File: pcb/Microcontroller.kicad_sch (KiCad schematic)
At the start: 39 parts, among them J1 PDI, SW2 START, SW3 STOP, U3 ATxmega16A4U-A, Y1 8MHz

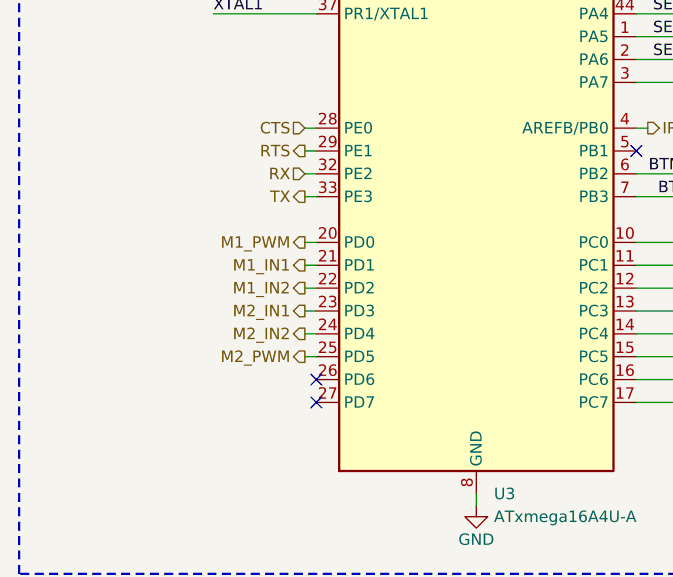
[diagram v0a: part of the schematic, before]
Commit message: [pcb] Line sensors placed
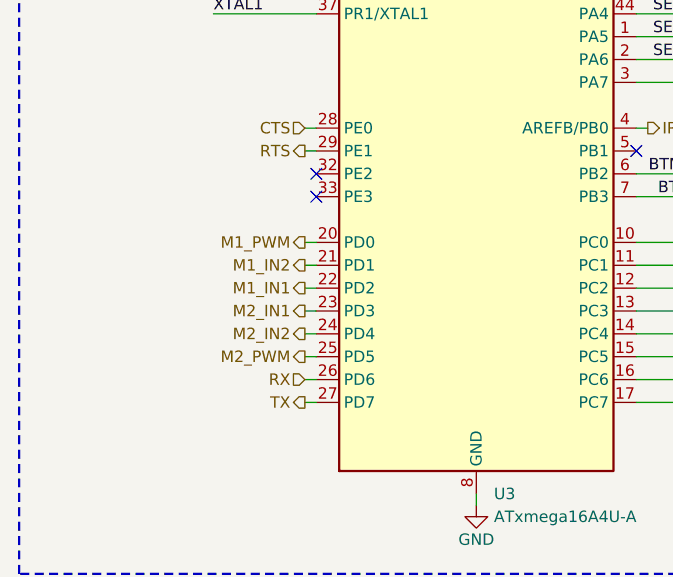
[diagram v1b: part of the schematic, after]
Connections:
- net M1_IN1: now also U3.22 (PD2); no longer U3.21 (PD1)
- net M1_IN2: now also U3.21 (PD1); no longer U3.22 (PD2)
- net RX: now also U3.26 (PD6); no longer U3.32 (PE2)
- net TX: now also U3.27 (PD7); no longer U3.33 (PE3)
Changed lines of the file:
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@@
   (junction (at 148.59 95.25) (diameter 0) (color 0 0 0 0)
   )
-  (no_connect (at 50.8 102.87))
   (no_connect (at 86.36 77.47))
+  (no_connect (at 50.8 80.01))
   (no_connect (at 135.89 39.37))
   (no_connect (at 148.59 39.37))
-  (no_connect (at 50.8 105.41))
+  (no_connect (at 50.8 82.55))
   (bus_entry (at 96.52 62.23) (size 2.54 -2.54)
     (stroke (width 0) (type default))
@@
     (stroke (width 0) (type default))
   )
+  (wire (pts (xy 49.53 102.87) (xy 50.8 102.87))
+    (stroke (width 0) (type default))
+  )
   (wire (pts (xy 49.53 46.99) (xy 49.53 52.07))
     (stroke (width 0) (type default))
@@
     (stroke (width 0) (type default))
   )
+  (wire (pts (xy 49.53 105.41) (xy 50.8 105.41))
+    (stroke (width 0) (type default))
+  )
   (bus (pts (xy 99.06 52.07) (xy 99.06 54.61))
     (stroke (width 0) (type default))
@@
     (stroke (width 0) (type default))
   )
-  (wire (pts (xy 49.53 82.55) (xy 50.8 82.55))
-    (stroke (width 0) (type default))
-  )
   (wire (pts (xy 205.74 49.53) (xy 218.44 49.53))
     (stroke (width 0) (type default))
@@
   )
   (wire (pts (xy 86.36 102.87) (xy 96.52 102.87))
-    (stroke (width 0) (type default))
-  )
-  (wire (pts (xy 49.53 80.01) (xy 50.8 80.01))
     (stroke (width 0) (type default))
   )
@@
     (effects (font (size 1.27 1.27)) (justify right))
   )
-  (hierarchical_label "RX" (shape input) (at 49.53 80.01 180) (fields_autoplaced)
+  (hierarchical_label "RX" (shape input) (at 49.53 102.87 180) (fields_autoplaced)
     (effects (font (size 1.27 1.27)) (justify right))
   )
@@
     (effects (font (size 1.27 1.27)) (justify right))
   )
-  (hierarchical_label "M1_IN2" (shape output) (at 49.53 92.71 180) (fields_autoplaced)
+  (hierarchical_label "M1_IN2" (shape output) (at 49.53 90.17 180) (fields_autoplaced)
     (effects (font (size 1.27 1.27)) (justify right))
   )
@@
     (effects (font (size 1.27 1.27)) (justify left))
   )
-  (hierarchical_label "TX" (shape output) (at 49.53 82.55 180) (fields_autoplaced)
+  (hierarchical_label "TX" (shape output) (at 49.53 105.41 180) (fields_autoplaced)
     (effects (font (size 1.27 1.27)) (justify right))
   )
@@
     (effects (font (size 1.27 1.27)) (justify left))
   )
-  (hierarchical_label "M1_IN1" (shape output) (at 49.53 90.17 180) (fields_autoplaced)
-    (effects (font (size 1.27 1.27)) (justify right))
-  )
+  (hierarchical_label "M1_IN1" (shape output) (at 49.53 92.71 180) (fields_autoplaced)
+    (effects (font (size 1.27 1.27)) (justify right))
+  )

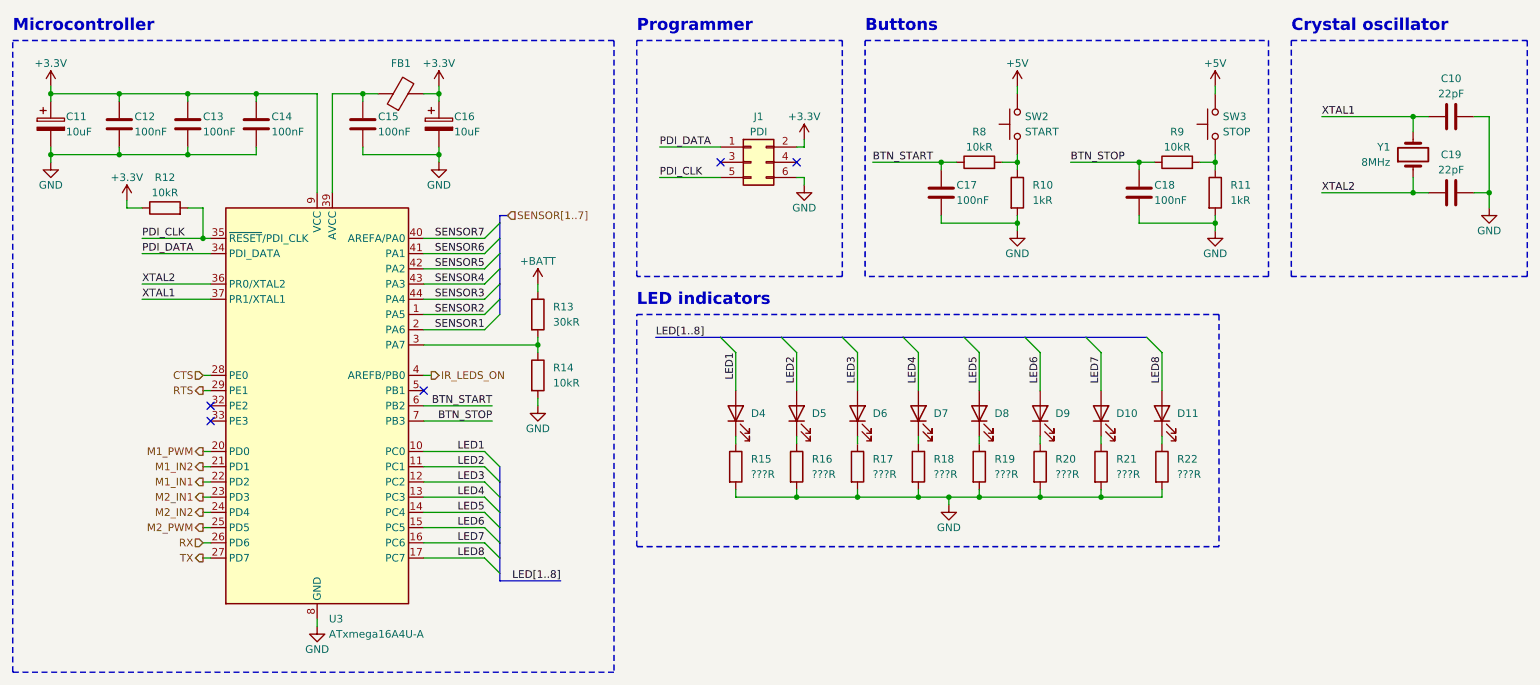
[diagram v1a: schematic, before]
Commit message: [pcb] Trying to minimize number of vias
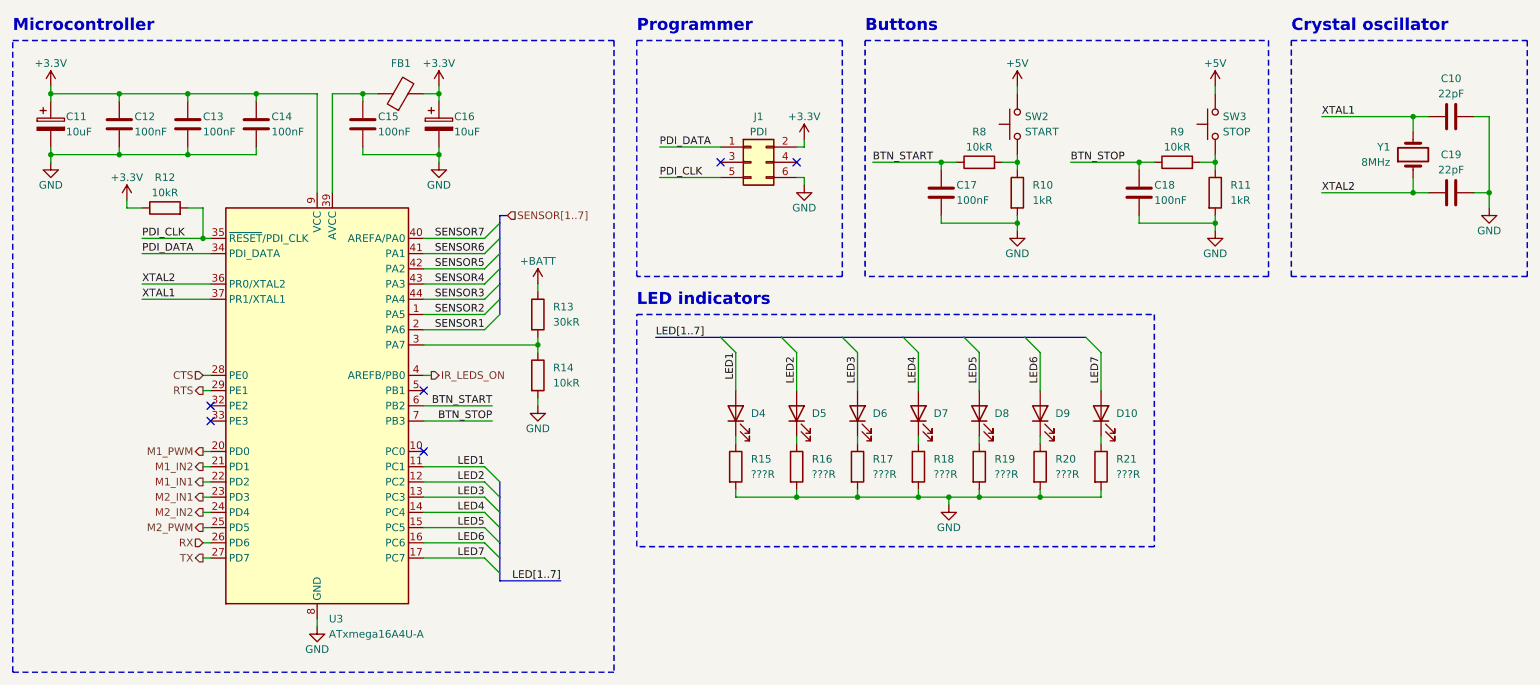
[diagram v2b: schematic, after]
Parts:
- removed D11: YELLOW, LED_SMD:LED_0805_2012Metric, symbol Device:LED
- removed R22: ???R, Resistor_SMD:R_0805_2012Metric, symbol Device:R
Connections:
- net LED8 is gone; now on net LED7: U3.17 (PC7)
- net LED1: now also U3.11 (PC1); no longer U3.10 (PC0)
- net LED2: now also U3.12 (PC2); no longer U3.11 (PC1)
- net LED3: now also U3.13 (PC3); no longer U3.12 (PC2)
- net LED4: now also U3.14 (PC4); no longer U3.13 (PC3)
- net LED5: now also U3.15 (PC5); no longer U3.14 (PC4)
- net LED6: now also U3.16 (PC6); no longer U3.15 (PC5)
- net LED7: no longer U3.16 (PC6)
- no-connect marks 5 -> 6

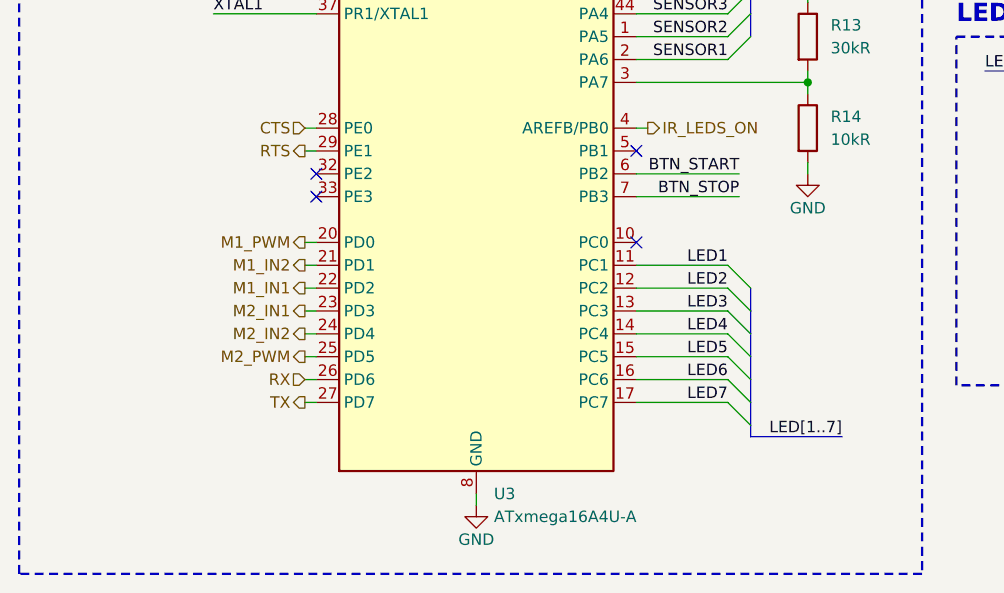
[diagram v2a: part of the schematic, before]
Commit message: [pcb] Rotate uC by 45 deg
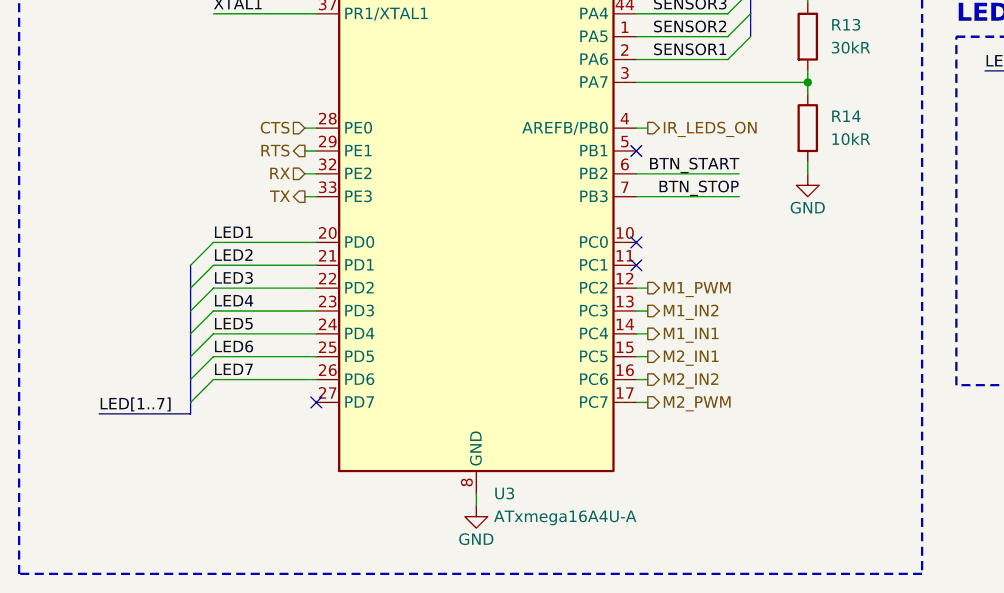
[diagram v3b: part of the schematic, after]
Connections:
- net LED1: now also U3.20 (PD0); no longer U3.11 (PC1)
- net LED2: now also U3.21 (PD1); no longer U3.12 (PC2)
- net LED3: now also U3.22 (PD2); no longer U3.13 (PC3)
- net LED4: now also U3.23 (PD3); no longer U3.14 (PC4)
- net LED5: now also U3.24 (PD4); no longer U3.15 (PC5)
- net LED6: now also U3.25 (PD5); no longer U3.16 (PC6)
- net LED7: now also U3.26 (PD6); no longer U3.17 (PC7)
- net M1_IN1: now also U3.14 (PC4); no longer U3.22 (PD2)
- net M1_IN2: now also U3.13 (PC3); no longer U3.21 (PD1)
- net M1_PWM: now also U3.12 (PC2); no longer U3.20 (PD0)
- net M2_IN1: now also U3.15 (PC5); no longer U3.23 (PD3)
- net M2_IN2: now also U3.16 (PC6); no longer U3.24 (PD4)
- net M2_PWM: now also U3.17 (PC7); no longer U3.25 (PD5)
- net RX: now also U3.32 (PE2); no longer U3.26 (PD6)
- net TX: now also U3.33 (PE3); no longer U3.27 (PD7)

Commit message: [pcb] Remove unnecessary capacitors
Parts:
- removed C11: 10uF, Capacitor_Tantalum_SMD:CP_EIA-3216-18_Kemet-A, symbol Device:C_Polarized
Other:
- moved on the sheet: R12
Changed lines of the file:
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@@
   (junction (at 88.9 38.1) (diameter 0) (color 0 0 0 0)
   )
+  (junction (at 35.56 27.94) (diameter 0) (color 0 0 0 0)
+  )
+  (junction (at 76.2 27.94) (diameter 0) (color 0 0 0 0)
+  )
+  (junction (at 251.46 31.75) (diameter 0) (color 0 0 0 0)
+  )
+  (junction (at 185.42 39.37) (diameter 0) (color 0 0 0 0)
+  )
+  (junction (at 58.42 27.94) (diameter 0) (color 0 0 0 0)
+  )
   (junction (at 35.56 38.1) (diameter 0) (color 0 0 0 0)
   )
-  (junction (at 76.2 27.94) (diameter 0) (color 0 0 0 0)
-  )
-  (junction (at 251.46 31.75) (diameter 0) (color 0 0 0 0)
-  )
-  (junction (at 185.42 39.37) (diameter 0) (color 0 0 0 0)
-  )
-  (junction (at 58.42 27.94) (diameter 0) (color 0 0 0 0)
-  )
   (junction (at 88.9 27.94) (diameter 0) (color 0 0 0 0)
   )
-  (junction (at 35.56 27.94) (diameter 0) (color 0 0 0 0)
-  )
   (junction (at 179.07 95.25) (diameter 0) (color 0 0 0 0)
   )
@@
   (junction (at 218.44 49.53) (diameter 0) (color 0 0 0 0)
   )
-  (junction (at 24.13 27.94) (diameter 0) (color 0 0 0 0)
-  )
   (junction (at 189.23 95.25) (diameter 0) (color 0 0 0 0)
   )
@@
   )
   (junction (at 185.42 49.53) (diameter 0) (color 0 0 0 0)
-  )
-  (junction (at 24.13 38.1) (diameter 0) (color 0 0 0 0)
   )
   (junction (at 148.59 95.25) (diameter 0) (color 0 0 0 0)
@@
     (stroke (width 0) (type default))
   )
-  (wire (pts (xy 24.13 27.94) (xy 24.13 29.21))
-    (stroke (width 0) (type default))
-  )
   (wire (pts (xy 35.56 27.94) (xy 46.99 27.94))
     (stroke (width 0) (type default))
@@
     (stroke (width 0) (type default))
   )
-  (wire (pts (xy 36.83 45.72) (xy 36.83 46.99))
+  (wire (pts (xy 24.13 46.99) (xy 24.13 48.26))
     (stroke (width 0) (type default))
   )
@@
     (stroke (width 0) (type default))
   )
-  (wire (pts (xy 24.13 38.1) (xy 24.13 39.37))
-    (stroke (width 0) (type default))
-  )
   (wire (pts (xy 158.75 93.98) (xy 158.75 95.25))
     (stroke (width 0) (type default))
@@
     (stroke (width 0) (type default))
   )
-  (wire (pts (xy 35.56 38.1) (xy 24.13 38.1))
-    (stroke (width 0) (type default))
-  )
   (wire (pts (xy 46.99 29.21) (xy 46.99 27.94))
     (stroke (width 0) (type default))
@@
     (stroke (width 0) (type default))
   )
-  (wire (pts (xy 46.99 46.99) (xy 49.53 46.99))
+  (wire (pts (xy 34.29 48.26) (xy 49.53 48.26))
     (stroke (width 0) (type default))
   )
@@
     (stroke (width 0) (type default))
   )
-  (wire (pts (xy 49.53 46.99) (xy 49.53 52.07))
+  (wire (pts (xy 49.53 48.26) (xy 49.53 52.07))
     (stroke (width 0) (type default))
   )
@@
     (stroke (width 0) (type default))
   )
-  (wire (pts (xy 24.13 27.94) (xy 35.56 27.94))
-    (stroke (width 0) (type default))
-  )
   (wire (pts (xy 86.36 82.55) (xy 97.79 82.55))
     (stroke (width 0) (type default))
@@
     (stroke (width 0) (type default))
   )
+  (wire (pts (xy 35.56 38.1) (xy 35.56 39.37))
+    (stroke (width 0) (type default))
+  )
   (wire (pts (xy 105.41 59.69) (xy 105.41 60.96))
     (stroke (width 0) (type default))
@@
     (stroke (width 0) (type default))
   )
-  (wire (pts (xy 24.13 36.83) (xy 24.13 38.1))
-    (stroke (width 0) (type default))
-  )
   (wire (pts (xy 179.07 95.25) (xy 189.23 95.25))
     (stroke (width 0) (type default))
@@
     (stroke (width 0) (type default))
   )
-  (wire (pts (xy 36.83 46.99) (xy 39.37 46.99))
+  (wire (pts (xy 24.13 48.26) (xy 26.67 48.26))
     (stroke (width 0) (type default))
   )
@@
     (stroke (width 0) (type default))
   )
+  (wire (pts (xy 35.56 26.67) (xy 35.56 27.94))
+    (stroke (width 0) (type default))
+  )
   (bus (pts (xy 36.83 95.25) (xy 36.83 97.79))
     (stroke (width 0) (type default))
@@
   )
   (wire (pts (xy 96.52 59.69) (xy 86.36 59.69))
-    (stroke (width 0) (type default))
-  )
-  (wire (pts (xy 24.13 26.67) (xy 24.13 27.94))
     (stroke (width 0) (type default))
   )
@@
     )
   )
-  (symbol (lib_id "power:GND") (at 24.13 39.37 0) (unit 1)
-    (in_bom yes) (on_board yes) (dnp no)
-    (property "Reference" "#PWR018" (at 24.13 45.72 0)
-      (effects (font (size 1.27 1.27)) hide)
-    )
-    (property "Value" "GND" (at 24.13 43.18 0)
-      (effects (font (size 1.27 1.27)))
-    )
-    (property "Footprint" "" (at 24.13 39.37 0)
-      (effects (font (size 1.27 1.27)) hide)
-    )
-    (property "Datasheet" "" (at 24.13 39.37 0)
+  (symbol (lib_id "power:GND") (at 35.56 39.37 0) (unit 1)
+    (in_bom yes) (on_board yes) (dnp no)
+    (property "Reference" "#PWR018" (at 35.56 45.72 0)
+      (effects (font (size 1.27 1.27)) hide)
+    )
+    (property "Value" "GND" (at 35.56 43.18 0)
+      (effects (font (size 1.27 1.27)))
+    )
+    (property "Footprint" "" (at 35.56 39.37 0)
+      (effects (font (size 1.27 1.27)) hide)
+    )
+    (property "Datasheet" "" (at 35.56 39.37 0)
       (effects (font (size 1.27 1.27)) hide)
     )
@@
     )
   )
-  (symbol (lib_id "Device:R") (at 43.18 46.99 90) (unit 1)
-    (in_bom yes) (on_board yes) (dnp no)
-    (property "Reference" "R12" (at 43.18 41.91 90)
-      (effects (font (size 1.27 1.27)))
-    )
-    (property "Value" "10kR" (at 43.18 44.45 90)
-      (effects (font (size 1.27 1.27)))
-    )
-    (property "Footprint" "Resistor_SMD:R_0805_2012Metric" (at 43.18 48.768 90)
-      (effects (font (size 1.27 1.27)) hide)
-    )
-    (property "Datasheet" "~" (at 43.18 46.99 0)
+  (symbol (lib_id "Device:R") (at 30.48 48.26 90) (unit 1)
+    (in_bom yes) (on_board yes) (dnp no)
+    (property "Reference" "R12" (at 30.48 43.18 90)
+      (effects (font (size 1.27 1.27)))
+    )
+    (property "Value" "10kR" (at 30.48 45.72 90)
+      (effects (font (size 1.27 1.27)))
+    )
+    (property "Footprint" "Resistor_SMD:R_0805_2012Metric" (at 30.48 50.038 90)
+      (effects (font (size 1.27 1.27)) hide)
+    )
+    (property "Datasheet" "~" (at 30.48 48.26 0)
       (effects (font (size 1.27 1.27)) hide)
     )
@@
     )
   )
-  (symbol (lib_id "Device:C_Polarized") (at 24.13 33.02 0) (unit 1)
-    (in_bom yes) (on_board yes) (dnp no)
-    (property "Reference" "C11" (at 26.67 31.75 0)
-      (effects (font (size 1.27 1.27)) (justify left))
-    )
-    (property "Value" "10uF" (at 26.67 34.29 0)
-      (effects (font (size 1.27 1.27)) (justify left))
-    )
-    (property "Footprint" "Capacitor_Tantalum_SMD:CP_EIA-3216-18_Kemet-A" (at 25.0952 36.83 0)
-      (effects (font (size 1.27 1.27)) hide)
-    )
-    (property "Datasheet" "~" (at 24.13 33.02 0)
-      (effects (font (size 1.27 1.27)) hide)
-    )
-    (pin "1")
-    (pin "2")
-    (instances
-      (project "Autko"
-        (path "/8d5cfdec-de34-4148-9100-7125640c46f5/bbdb254f-809b-458f-9d25-868d15ad41c7"
-          (reference "C11") (unit 1)
-        )
-      )
-    )
-  )
-  (symbol (lib_id "power:+3.3V") (at 36.83 45.72 0) (unit 1)
+  (symbol (lib_id "power:+3.3V") (at 24.13 46.99 0) (unit 1)
     (in_bom yes) (on_board yes) (dnp no) (fields_autoplaced)
-    (property "Reference" "#PWR021" (at 36.83 49.53 0)
-      (effects (font (size 1.27 1.27)) hide)
-    )
-    (property "Value" "+3.3V" (at 36.83 41.91 0)
-      (effects (font (size 1.27 1.27)))
-    )
-    (property "Footprint" "" (at 36.83 45.72 0)
-      (effects (font (size 1.27 1.27)) hide)
-    )
-    (property "Datasheet" "" (at 36.83 45.72 0)
+    (property "Reference" "#PWR021" (at 24.13 50.8 0)
+      (effects (font (size 1.27 1.27)) hide)
+    )
+    (property "Value" "+3.3V" (at 24.13 43.18 0)
+      (effects (font (size 1.27 1.27)))
+    )
+    (property "Footprint" "" (at 24.13 46.99 0)
+      (effects (font (size 1.27 1.27)) hide)
+    )
+    (property "Datasheet" "" (at 24.13 46.99 0)
       (effects (font (size 1.27 1.27)) hide)
     )
@@
     )
   )
-  (symbol (lib_id "power:+3.3V") (at 24.13 26.67 0) (unit 1)
+  (symbol (lib_id "power:+3.3V") (at 35.56 26.67 0) (unit 1)
     (in_bom yes) (on_board yes) (dnp no) (fields_autoplaced)
-    (property "Reference" "#PWR013" (at 24.13 30.48 0)
-      (effects (font (size 1.27 1.27)) hide)
-    )
-    (property "Value" "+3.3V" (at 24.13 22.86 0)
-      (effects (font (size 1.27 1.27)))
-    )
-    (property "Footprint" "" (at 24.13 26.67 0)
-      (effects (font (size 1.27 1.27)) hide)
-    )
-    (property "Datasheet" "" (at 24.13 26.67 0)
-      (effects (font (size 1.27 1.27)) hide)
-    )
+    (property "Reference" "#PWR013" (at 35.56 30.48 0)
+      (effects (font (size 1.27 1.27)) hide)
+    )
+    (property "Value" "+3.3V" (at 35.56 22.86 0)
+      (effects (font (size 1.27 1.27)))
+    )
+    (property "Footprint" "" (at 35.56 26.67 0)
+      (effects (font (size 1.27 1.27)) hide)
+    )
+    (property "Datasheet" "" (at 35.56 26.67 0)
+      (effects (font (size 1.27 1.27)) hide)
+    )
